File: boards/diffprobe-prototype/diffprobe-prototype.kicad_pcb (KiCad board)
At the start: 4 copper layers, 41 x 35 mm, 49 parts, among them K1 CUI PJ-058BH, K2 CUI PJ-058BH, P1 SMA, P10 TESTCLIP, P11 SMA, P2 SMA, P3 TESTPOINT, P4 TESTPOINT, P5 TESTCLIP, P6 TESTCLIP, P7 TESTCLIP, P8 TESTCLIP, P9 TESTCLIP, U1 LT3032IDE-5#PBF, U2 THS3217

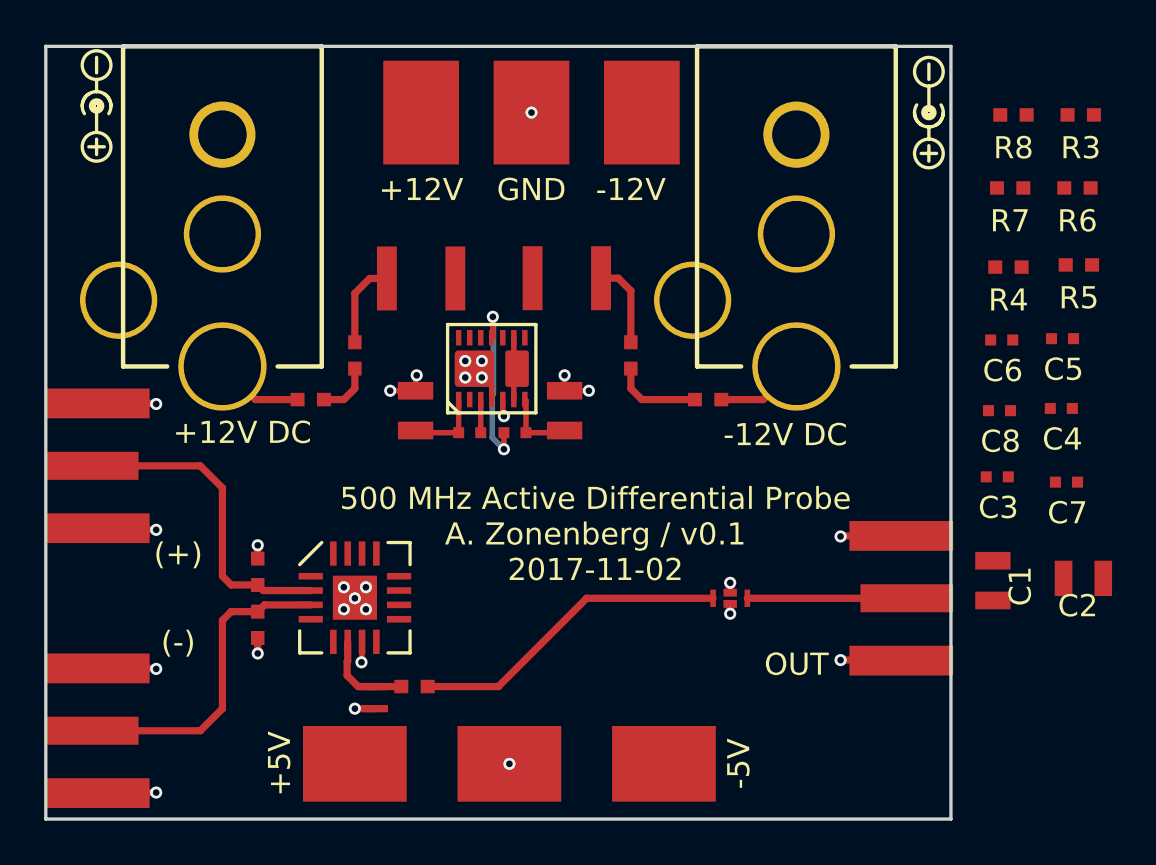
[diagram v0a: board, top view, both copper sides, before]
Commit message: Finished initial layout. Still needs layout review before tapeout.
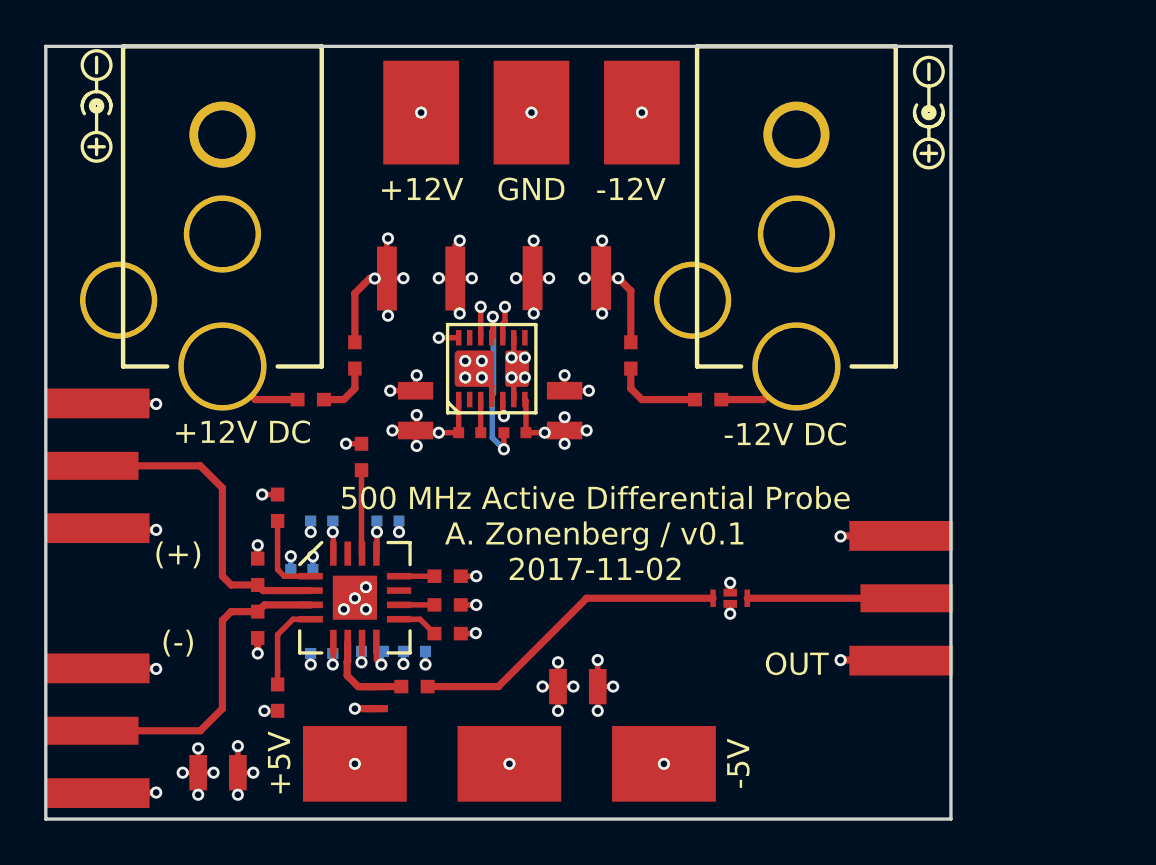
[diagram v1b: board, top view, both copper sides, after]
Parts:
- C3, C4, C5, C6, C7, C8: moved to B.Cu
- moved R3 40.5 mm to (137.5, 63.9), turned to 270 degrees
- moved R7 40.4 mm to (137.5, 72.5), turned to 90 degrees
- moved C1 36.2 mm to (134.8, 75.9), turned to 180 degrees
- moved C7 34.9 mm to (138.6, 66.7)
- moved R6 34.6 mm to (141.3, 61.6), turned to 270 degrees
- moved C5 34.6 mm to (139.5, 64.5), turned to 180 degrees
- moved R8 33.9 mm to (145.2, 68.3), turned to 180 degrees
- moved C8 32.6 mm to (139.5, 70.5)
- moved R5 31.9 mm to (145.2, 67.0), turned to 180 degrees
- moved C6 31.8 mm to (141.8, 70.4)
- moved C4 31.3 mm to (143.7, 70.4)
- moved R4 30.3 mm to (145.2, 69.6), turned to 180 degrees
- moved C3 27.7 mm to (142.5, 64.5)
- moved C2 23.4 mm to (151.1, 72.0)
- moved G*** 4.00 mm to (140.0, 45.8)
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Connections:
- R7 pad 1: /5V0 -> /5V0_P
- R8 pad 1: /5V0 -> /5V0_P
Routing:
- net /GND: track 184.0 -> 248.5 mm, vias 28 -> 52
- net /5V0_P: track 3.49 -> 52.5 mm, vias 0 -> 13
- net /5V0_N: track 3.31 -> 50.4 mm, vias 0 -> 11
- net /12V0_P: track 3.94 -> 32.7 mm, vias 0 -> 8
- net /12V0_N: track 6.84 -> 32.3 mm, vias 0 -> 9
- net Net-(R7-Pad2): track 0.00 -> 4.04 mm
- net Net-(R3-Pad2): track 0.00 -> 3.83 mm
- net Net-(R6-Pad2): track 0.00 -> 3.79 mm
- net Net-(R4-Pad2): track 0.00 -> 1.87 mm
- net Net-(R8-Pad2): track 0.00 -> 1.60 mm
- net Net-(R5-Pad2): track 0.00 -> 1.60 mm
- added copper zone on In2.Cu, net /12V0_N
- added copper zone on In2.Cu, net /12V0_P
- added copper zone on In2.Cu, net /5V0_N
- added copper zone on In2.Cu, net /5V0_P
- added copper zone on In1.Cu, net /GND

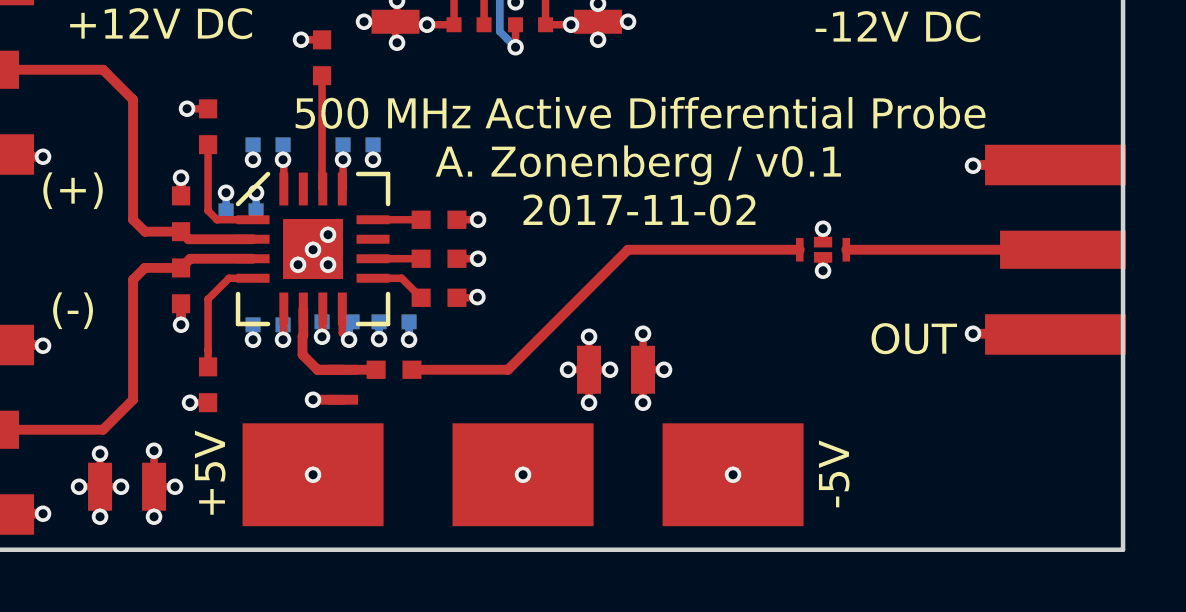
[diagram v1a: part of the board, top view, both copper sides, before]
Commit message: Continued design review. Added output directory.
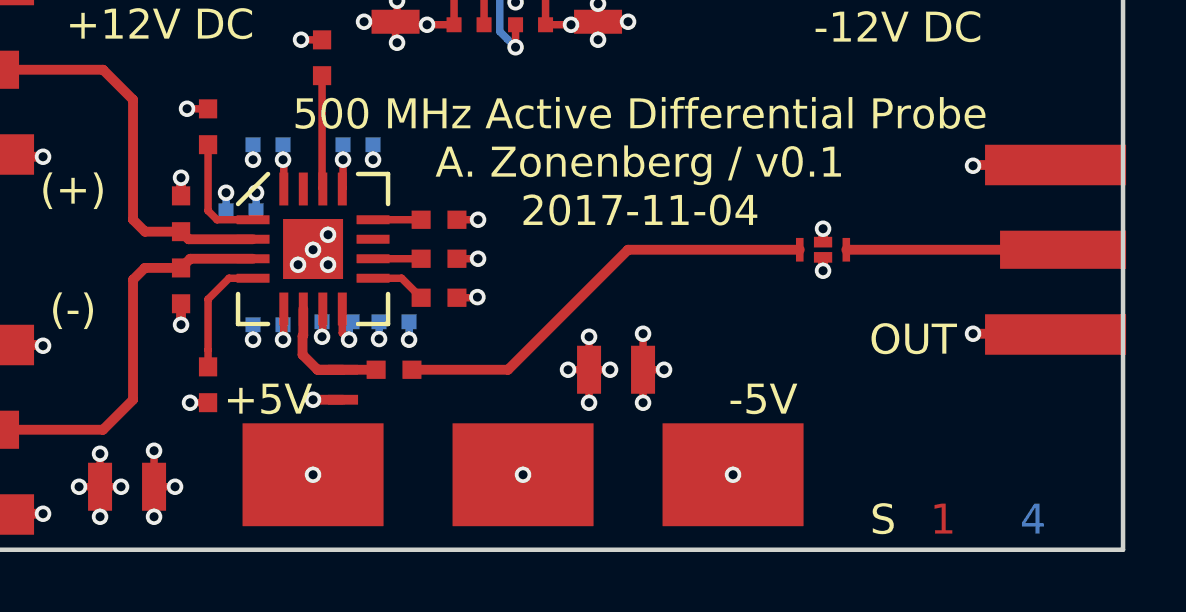
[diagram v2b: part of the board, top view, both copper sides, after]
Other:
- board text added: "1"
- board text added: "2"
- board text added: "3"
- board text added: "4"
- board text added: "500 MHz Active Differential Probe A. Zonenberg / v0.1 2017-11-04"
- board text added: "M"
- board text added: "S"
- board text removed: "500 MHz Active Differential Probe A. Zonenberg / v0.1 2017-11-02"
